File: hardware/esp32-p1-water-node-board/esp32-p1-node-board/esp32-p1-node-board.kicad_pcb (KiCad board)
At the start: 2 copper layers, 108 x 57.5 mm, 17 parts, among them J1 RJ11-6, Q1 BC847, Q2 BSS138, U1 TTGO_LoRa32_V11

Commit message: Update
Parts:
- removed C1: 10n, Capacitor_SMD:C_1206_3216Metric
- removed JP1, JP3: Serial-type-select, Jumpers:SMT-JUMPER_3_1-NC_TRACE_SILK
- removed JP2: Data-request-select, Jumpers:SMT-JUMPER_3_1-NC_TRACE_SILK
- removed R3: 12K, Resistor_SMD:R_1206_3216Metric
- added D2: BAT54S, Package_TO_SOT_SMD:SOT-23, F.Cu at (86.0, 45.3)
- Q1: value BC847 -> BSS138
- R2: value 1K -> 10K
- moved Q1 62.8 mm to (86.0, 49.7)
- moved R5 62.2 mm to (89.0, 61.5), turned to 0 degrees
- moved Q2 61.1 mm to (83.7, 63.2), turned to 0 degrees
- moved D1 57.9 mm to (83.7, 58.8), turned to 0 degrees
- moved R4 48.2 mm to (89.0, 58.2), turned to 0 degrees
- moved R2 38.5 mm to (91.2, 48.0), turned to 0 degrees
- moved R1 33.5 mm to (91.2, 44.7), turned to 0 degrees
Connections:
- net Net-(Q2-S) renamed /DATA_P1_3V3
- C2 pad 2: /DATA_GND -> /GND
- C3 pad 1: /DATA_GND -> /GND
- Conn1 pad 5: /DATA_GND -> /GND
- D1 pad 1: /DATA_GND -> /DATA_P1_GND
- D1 pad 3: /DATA_5V_R -> /DATA_P1
- J1 pad 2: /DATA_REQ -> /DATA_P1_REQ
- J1 pad 3: /DATA_GND -> /DATA_P1_GND
- J1 pad 5: /DATA -> /DATA_P1
- J1 pad 6: /DATA_GND -> /GND
- Q1 pad 1: /DATA_5V_R -> Net-(Q1-G)
- Q1 pad 2: /DATA_GND -> /PULSE_WATER_3V3
- Q1 pad 3: /DATA_3V3_N -> /PULSE_WATER
- Q2 pad 1: /3V3 -> Net-(Q2-G)
- Q2 pad 3: /DATA_5V_R -> /DATA_P1
- R1 pad 1: /5V -> unconnected-(R1-Pad1)
- R1 pad 2: /DATA -> /PULSE_WATER
- R2 pad 1: /DATA_5V_R -> Net-(Q1-G)
- R2 pad 2: /DATA -> /PULSE_WATER_3V3
- R4 pad 1: /5V -> unconnected-(R4-Pad1)
- R4 pad 2: /DATA_5V_R -> /DATA_P1
- R5 pad 1: /3V3 -> Net-(Q2-G)
- U1 pad 1: /DATA_GND -> unconnected-(U1-GND-Pad1)
- U1 pad 2: /5V -> unconnected-(U1-5V-Pad2)
- U1 pad 3: /3V3 -> unconnected-(U1-3V3-Pad3)
- U1 pad 34: /3V3 -> unconnected-(U1-3V3-Pad34)
- U1 pad 35: /5V -> unconnected-(U1-5V-Pad35)
- U1 pad 36: /DATA_GND -> unconnected-(U1-GND-Pad36)
- U1 pad 4: /DATA_GND -> unconnected-(U1-GND-Pad4)
- U1 pad 5: /HARD_RXD -> unconnected-(U1-GPIO03-Pad5)
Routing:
- net /5V: track 165.7 -> 5.85 mm
- net /3V3: track 117.1 -> 0.00 mm, vias 2 -> 0
- net /DATA_REQ: track 49.1 -> 0.00 mm, vias 2 -> 0
- net /DATA_GND: track 39.8 -> 0.00 mm, vias 2 -> 0
- net /DATA_5V_R: track 33.6 -> 0.00 mm
- net /DATA_P1_3V3: track 27.4 -> 0.00 mm
- net /DATA: track 19.9 -> 0.00 mm
- net /DATA_3V3: track 18.5 -> 0.00 mm
- net /DATA_3V3_N: track 18.0 -> 0.00 mm
- net /SOFT_REQ: track 15.3 -> 0.00 mm
- net /HARD_RXD: track 15.1 -> 0.00 mm
- net /SOFT_RXD: track 13.4 -> 0.00 mm
- net /GND: track 0.00 -> 3.45 mm
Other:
- board text removed: "Continous"
- board text removed: "Controlled"
- board text removed: "Hard-serial"
- board text removed: "Normal"
- board text removed: "Opt: Level-inverter"
- board text removed: "Reverse"
- board text removed: "Soft-serial"

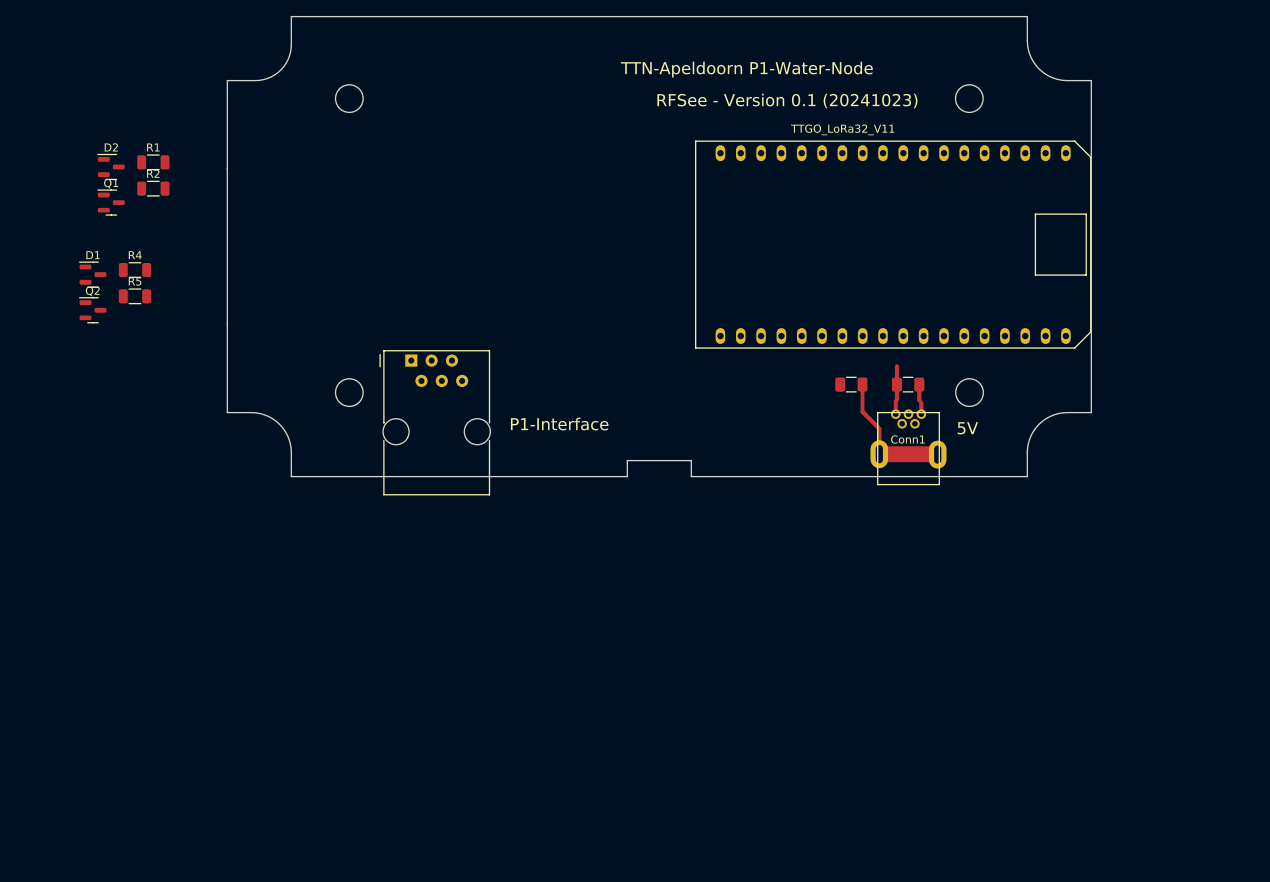
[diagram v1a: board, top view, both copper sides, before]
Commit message: Updated files to KiCad 8.0
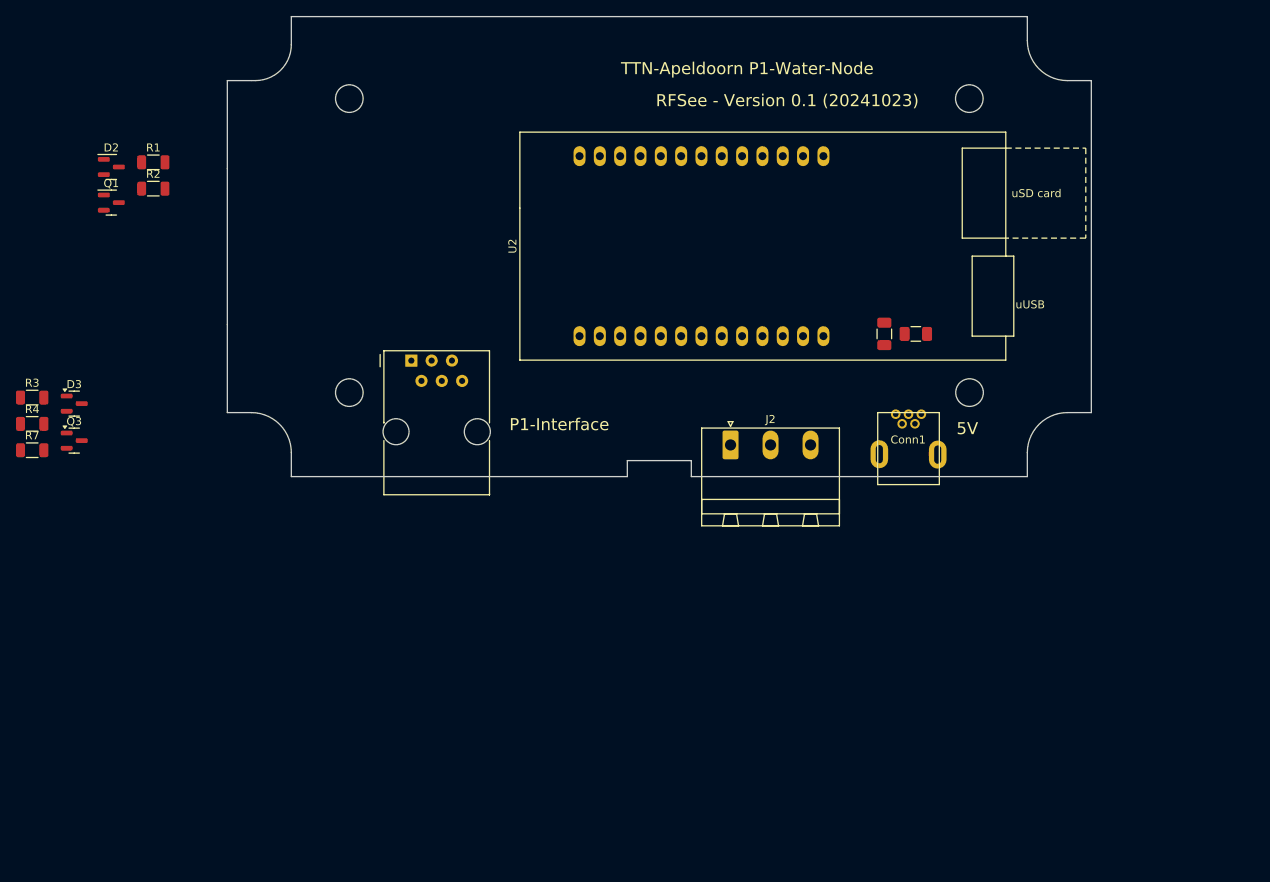
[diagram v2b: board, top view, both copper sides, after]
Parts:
- removed D1: BAT54S, Package_TO_SOT_SMD:SOT-23
- removed Q2: BSS138, Package_TO_SOT_SMD:SOT-23
- removed R5: 10K, Resistor_SMD:R_1206_3216Metric
- removed U1: TTGO_LoRa32_V11, esp32-p1-node-board:TTGO_LoRa32_V11
- added D3: BAT54S, Package_TO_SOT_SMD:SOT-23, F.Cu at (81.4, 74.9)
- added J2: Conn_01x03, Connector_Phoenix_MSTB:PhoenixContact_MSTBA_2,5_3-G_1x03_P5.00mm_Horizontal, F.Cu at (163.4, 80.0)
- added Q3: BC847, Package_TO_SOT_SMD:SOT-23, F.Cu at (81.4, 79.5)
- added R3: 10K, Resistor_SMD:R_1206_3216Metric, F.Cu at (76.1, 74.1)
- added R7: 12K, Resistor_SMD:R_1206_3216Metric, F.Cu at (76.1, 80.7)
- added U2: ~, my-KiCad-library:TTGO_T3_V1.6.1, F.Cu at (159.8, 55.2)
- R4: value 10K -> 1K
- moved R4 23.1 mm to (76.1, 77.4)
- moved C3 7.56 mm to (182.6, 66.2), turned to -90 degrees
- moved C2 6.41 mm to (186.6, 66.2)
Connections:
- C2 pad 2: /GND -> /DATA_P1_GND
- C3 pad 1: /GND -> /DATA_P1_GND
- Conn1 pad 5: /GND -> /DATA_P1_GND
- D2 pad 1: /PULSE_WATER_GND -> /DATA_P1_GND
- J1 pad 6: /GND -> /DATA_P1_GND
- R4 pad 1: unconnected-(R4-Pad1) -> Net-(Q3-B)
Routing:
- net Net-(C3-Pad2): track 16.9 -> 0.07 mm
- net /5V: track 5.85 -> 0.00 mm
- net /GND: track 3.45 -> 0.00 mm

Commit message: Start design PCB
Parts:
- added C1: 22n, Capacitor_SMD:C_1206_3216Metric, F.Cu at (141.7, 95.8)
- added D1: BAT54S, Package_TO_SOT_SMD:SOT-23, F.Cu at (134.7, 95.7)
- added Q2: BSS138, Package_TO_SOT_SMD:SOT-23, F.Cu at (148.5, 87.3)
- added R5: 10K, Resistor_SMD:R_1206_3216Metric, F.Cu at (152.5, 87.4)
- added R6: 10K, Resistor_SMD:R_1206_3216Metric, F.Cu at (144.8, 95.8)
- added R8: 10K, Resistor_SMD:R_1206_3216Metric, F.Cu at (141.8, 87.4)
- added R9: 10K, Resistor_SMD:R_1206_3216Metric, F.Cu at (138.6, 95.8)
- Q3: value BC847 -> BSS138
- R3: value 10K -> 2K7
- R4: value 1K -> 10K
- R7: value 12K -> 10K
- moved R2 83.0 mm to (152.4, 104.1), turned to 90 degrees
- moved Q1 82.8 mm to (148.4, 104.1), turned to 180 degrees
- moved R7 77.8 mm to (152.5, 95.8), turned to 90 degrees
- moved D2 76.4 mm to (134.7, 104.1), turned to 180 degrees
- moved R1 76.0 mm to (138.7, 104.1), turned to -90 degrees
- moved R4 69.5 mm to (144.9, 87.4), turned to -90 degrees
- moved Q3 69.2 mm to (148.6, 95.7), turned to 180 degrees
- moved R3 64.0 mm to (138.8, 87.4), turned to -90 degrees
- moved D3 54.8 mm to (134.8, 87.3), turned to 180 degrees
- moved C2 52.1 mm to (205.2, 114.8)
- moved C3 51.5 mm to (199.6, 114.8), turned to 180 degrees
- moved J2 46.6 mm to (182.7, 122.5)
- moved U2 46.6 mm to (179.1, 97.6)
- moved Conn1 46.6 mm to (208.8, 127.4)
- moved J1 46.6 mm to (142.8, 111.9)
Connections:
- Q1 pad 1: Net-(Q1-G) -> /3V3
- Q3 pad 1: Net-(Q3-B) -> /3V3
- Q3 pad 2: /DATA_P1_GND -> /DATA_P1_REQ_3V3
- Q3 pad 3: /DATA_P1_3V3 -> Net-(Q3-D)
- R1 pad 1: unconnected-(R1-Pad1) -> /5V
- R2 pad 1: Net-(Q1-G) -> /3V3
- R4 pad 1: Net-(Q3-B) -> /5V
- R4 pad 2: /DATA_P1 -> Net-(Q2-D)
- R7 pad 2: /DATA_P1_3V3 -> /DATA_P1_REQ_3V3
- U2 pad 15: /DATA_P1_REQ -> /PULSE_WATER_3V3
- U2 pad 17: /PULSE_WATER_3V3 -> unconnected-(U2-IO02-Pad17)
- U2 pad 21: unconnected-(U2-IO14-Pad21) -> /DATA_P1_REQ_3V3
- U2 pad 23: unconnected-(U2-IO34-Pad23) -> /DATA_P1_3V3
- U2 pad 3: /DATA_P1_3V3 -> unconnected-(U2-RXD-Pad3)
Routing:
- net /5V: track 0.00 -> 180.7 mm, vias 0 -> 2
- net /DATA_P1: track 0.00 -> 64.0 mm
- net /DATA_P1_REQ: track 0.00 -> 36.0 mm
- net /DATA_P1_GND: track 0.00 -> 27.9 mm
- net Net-(Q3-D): track 0.00 -> 12.5 mm
- net Net-(Q2-D): track 0.00 -> 9.37 mm
- net /3V3: track 0.00 -> 6.47 mm
- net /DATA_P1_3V3: track 0.00 -> 3.22 mm
- net /DATA_P1_REQ_3V3: track 0.00 -> 3.10 mm
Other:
- outline, holes or cut-outs redrawn
- board text added: "RFSee - Version 0.2 (20241117)"
- board text removed: "RFSee - Version 0.1 (20241023)"

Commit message: Final PCB design voor proef
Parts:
- added G***: LOGO_TTN-Apeldoorn, my-KiCad-library:LOGO_TTN-Apeldoorn, F.Cu at (166.9, 98.0)
- added G***: LOGO_LogoRFSee_28x5-6mm, my-KiCad-library:LOGO_LogoRFSee_28x5-6mm, F.Cu at (193.8, 101.1)
- renumbered D3 to D1, D1 to D3, Q2 to Q1, Q1 to Q2, R3 to R1, R8 to R2, R5 to R3, R1 to R5, R9 to R6, R6 to R7, R2 to R8, R7 to R9, U2 to U1
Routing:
- net /DATA_P1_GND: track 27.9 -> 160.0 mm, vias 0 -> 186
- net /PULSE_WATER: track 0.00 -> 66.9 mm
- net /3V3: track 6.47 -> 71.0 mm, vias 0 -> 3
- net /PULSE_WATER_3V3: track 0.00 -> 52.9 mm
- net /DATA_P1_REQ_3V3: track 3.10 -> 36.4 mm
- net /DATA_P1_3V3: track 3.22 -> 28.5 mm
- net Net-(C3-Pad2): track 0.07 -> 18.6 mm
- net /5V: track 180.7 -> 170.5 mm, vias 2 -> 3
- net /DATA_P1_REQ: track 36.0 -> 32.9 mm
- net /DATA_P1: track 64.0 -> 61.5 mm
- added copper zone on B.Cu, net /DATA_P1_GND
- added copper zone on F.Cu, net /DATA_P1_GND
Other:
- board text added: "GND"
- board text added: "Pulse"
- board text added: "Pulse-Interface"
- board text added: "RFSee - Version 0.3 (20241118)"
- board text removed: "RFSee - Version 0.2 (20241117)"

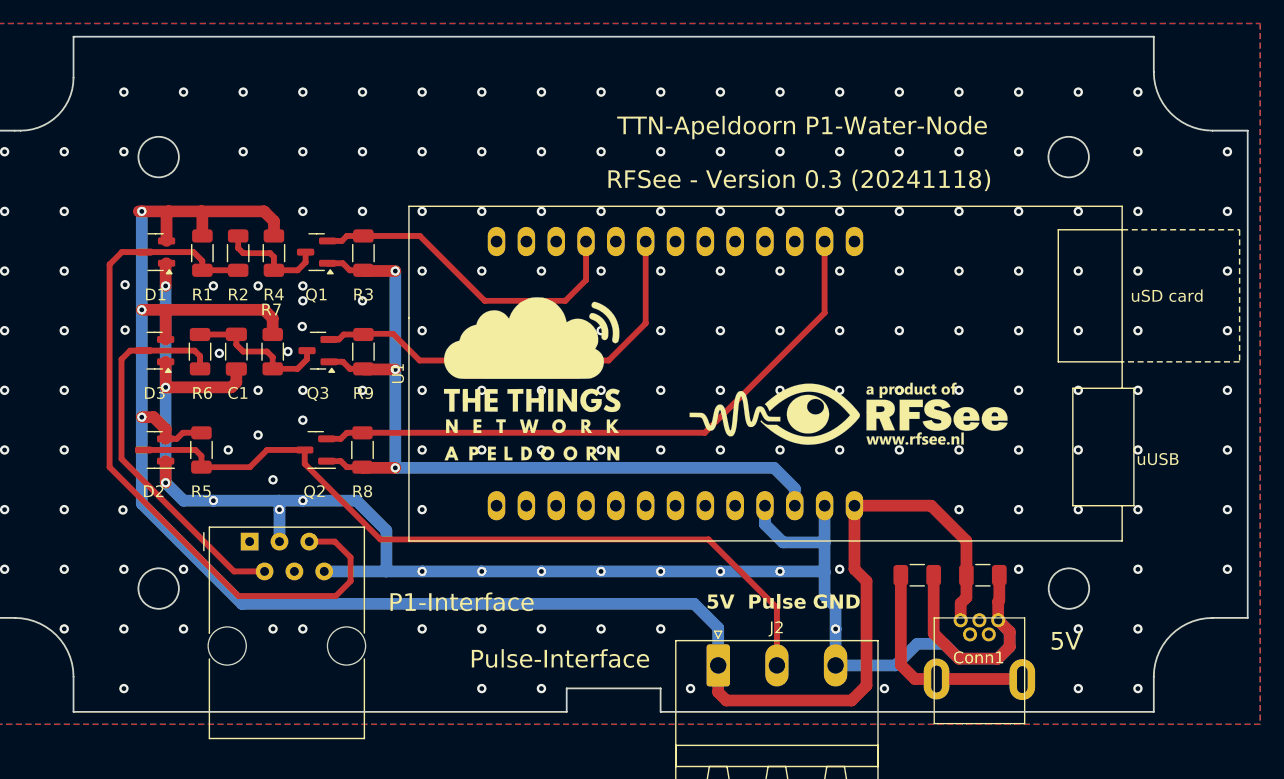
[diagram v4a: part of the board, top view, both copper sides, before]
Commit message: Updated PCB to version 0.5
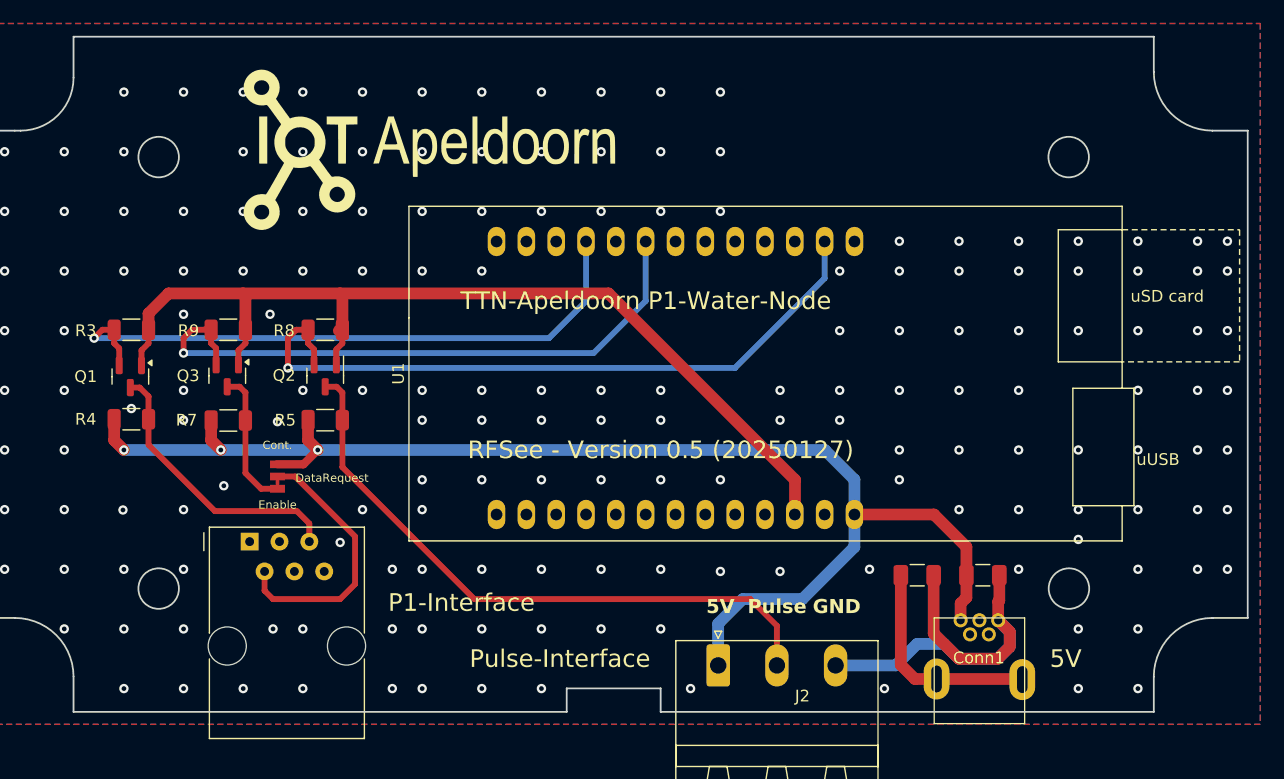
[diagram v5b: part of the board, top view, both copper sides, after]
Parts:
- removed C1: 22n, Capacitor_SMD:C_1206_3216Metric
- removed D1, D2, D3: BAT54S, Package_TO_SOT_SMD:SOT-23
- removed the G*** at (166.9, 98.0)
- removed the G*** at (193.8, 101.1)
- removed R1: 2K7, Resistor_SMD:R_1206_3216Metric
- removed R2, R6: 10K, Resistor_SMD:R_1206_3216Metric
- added G***: LOGO, my-KiCad-library:IOT-Apeldoorn_Logo, F.Cu at (157.5, 78.7)
- added JP1: ~, Sparkfun Jumpers:Jumper_3_NC-1_Trace_NoSilk, F.Cu at (145.2, 106.4)
- added REF**: KiCad-Logo2_12mm_SilkScreen, Symbol:KiCad-Logo2_12mm_SilkScreen, B.Cu at (146.6, 96.4)
- added REF**: OSHW-Logo_7.5x8mm_SilkScreen, Symbol:OSHW-Logo_7.5x8mm_SilkScreen, B.Cu at (171.4, 94.0)
- moved R3 20.8 mm to (132.7, 93.9), turned to 180 degrees
- moved Q1 19.1 mm to (132.6, 97.9), turned to -90 degrees
- moved R4 18.6 mm to (132.7, 101.5), turned to 0 degrees
- moved R9 11.7 mm to (141.0, 93.9), turned to 180 degrees
- moved R5 10.8 mm to (149.2, 101.6), turned to 0 degrees
- moved R8 10.7 mm to (149.2, 93.9), turned to 180 degrees
- moved Q3 8.02 mm to (140.9, 97.8), turned to -90 degrees
- moved R7 6.97 mm to (141.0, 101.6), turned to 0 degrees
- moved Q2 6.37 mm to (149.2, 97.8), turned to -90 degrees
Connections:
- Q1 pad 3: Net-(Q2-D) -> /DATA_P1
- R4 pad 2: Net-(Q2-D) -> /DATA_P1
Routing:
- net /DATA_P1_GND: track 160.0 -> 38.5 mm, vias 186 -> 173
- net /5V: track 170.5 -> 116.6 mm
- net /DATA_P1: track 61.5 -> 24.0 mm
- net /DATA_P1_3V3: track 28.5 -> 53.5 mm, vias 0 -> 1
- net /DATA_P1_REQ_3V3: track 36.4 -> 53.4 mm, vias 0 -> 1
- net /PULSE_WATER: track 66.9 -> 54.0 mm
- net /3V3: track 71.0 -> 82.8 mm, vias 3 -> 0
- net /DATA_P1_REQ: track 32.9 -> 22.9 mm
- net Net-(Q2-D): track 9.37 -> 0.00 mm
- net /PULSE_WATER_3V3: track 52.9 -> 59.7 mm, vias 0 -> 1
- net Net-(JP1-A): track 12.5 -> 11.9 mm
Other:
- board text added: "Cont."
- board text added: "DataRequest"
- board text added: "Enable"
- board text added: "RFSee - Version 0.5 (20250127)"
- board text removed: "RFSee - Version 0.3 (20241118)"
